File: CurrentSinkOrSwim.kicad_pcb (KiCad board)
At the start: 2 copper layers, 41.7 x 48.5 mm, 26 parts, among them P1 HEATSINK, P101 CONN_01X02, P102 CONN_01X03, P103 CONN_01X02, Q401 BUK9575, U201 LMV358, U301 LM2931

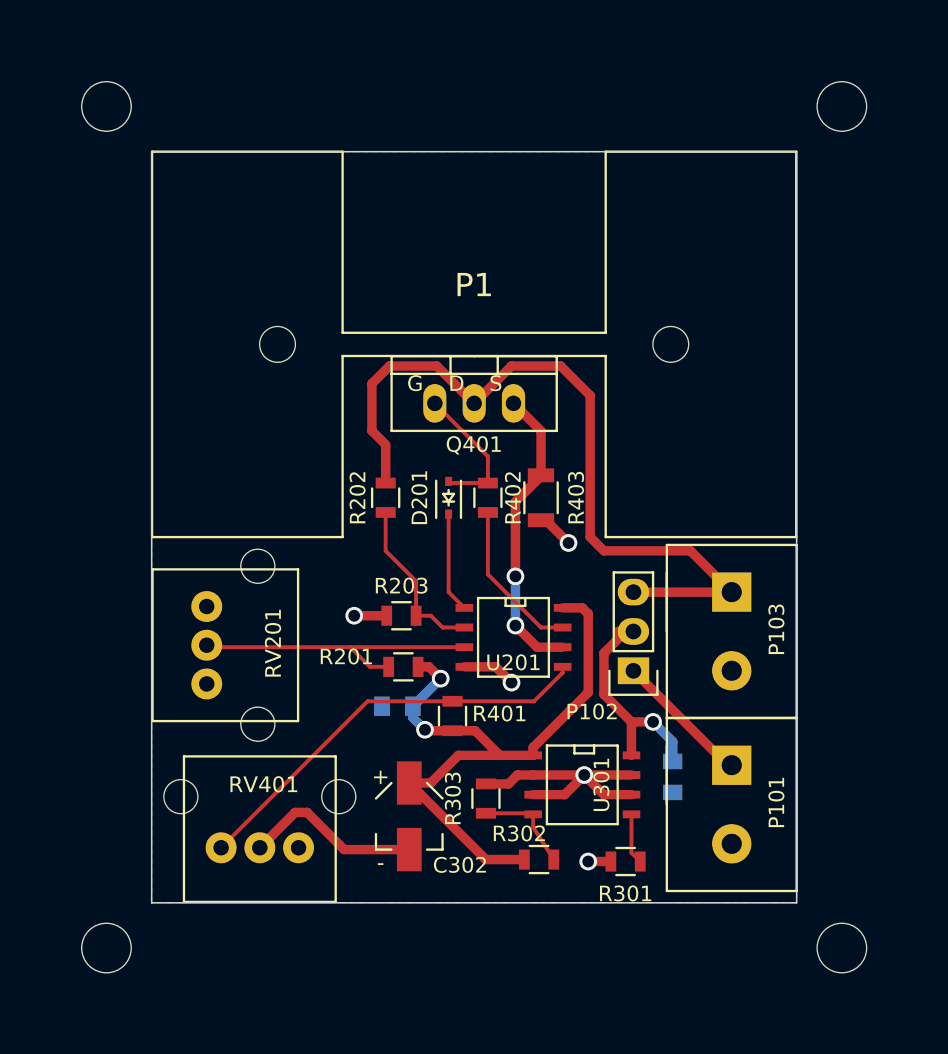
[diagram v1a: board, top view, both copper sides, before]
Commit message: added labels, switched leads on voltage pot so + == clockwise, enlarged ground plane
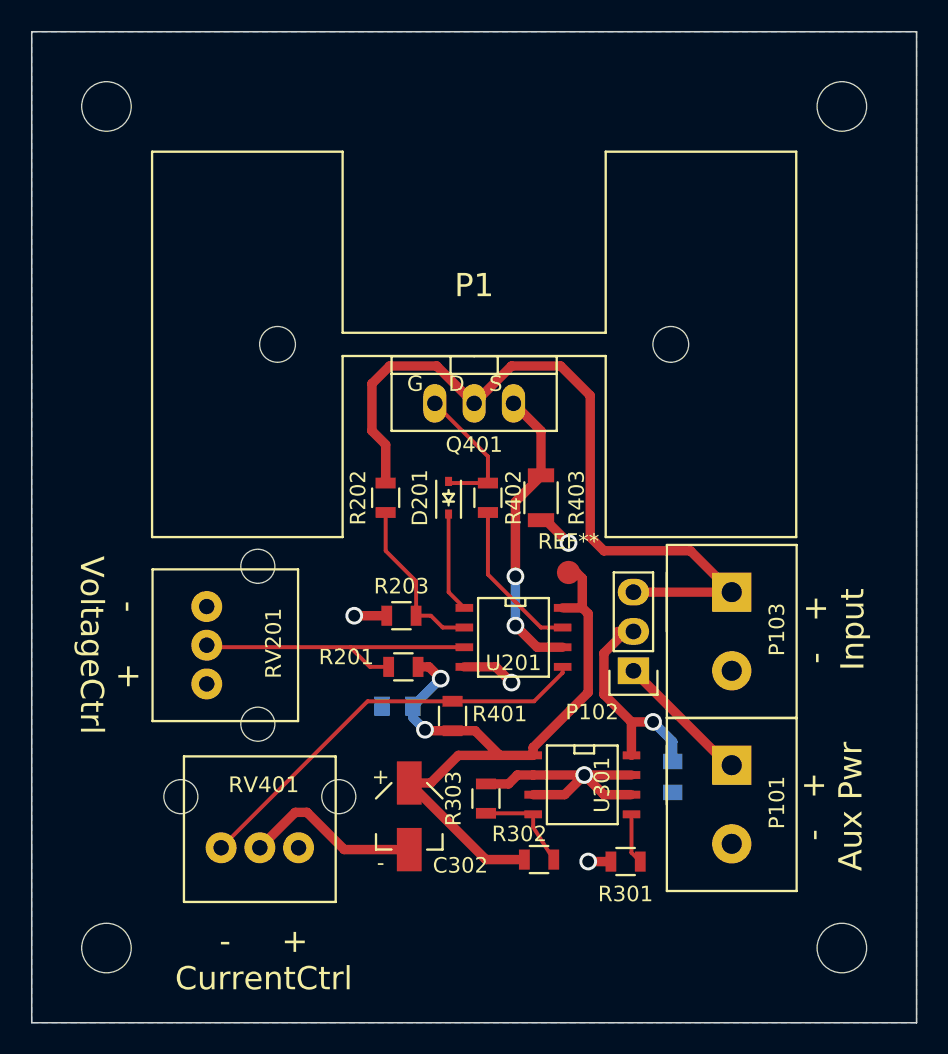
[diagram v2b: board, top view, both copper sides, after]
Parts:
- added REF**: Measurement_Point_Round-SMD-Pad_Small, Measurement_Points:Measurement_Point_Round-SMD-Pad_Small, F.Cu at (133.1, 63.0)
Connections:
- RV201 pad 1: Net-(RV201-Pad1) -> GND
- RV201 pad 3: GND -> Net-(RV201-Pad3)
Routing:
- net 2.7V: track 42.3 -> 45.3 mm
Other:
- board size 41.7 x 48.5 mm -> 57.1 x 64 mm
- board text added: "- + Aux Pwr"
- board text added: "- + CurrentCtrl"
- board text added: "- + Input"
- board text added: "- + VoltageCtrl"
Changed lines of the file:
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@@
 (kicad_pcb (version 4) (host pcbnew 4.0.2-stable)
   (general
-    (links 42)
+    (links 43)
     (no_connects 0)
-    (area 93.260057 27.2092 160.612943 92.5288)
+    (area 93.514057 27.4632 160.485943 92.5288)
     (thickness 1.6)
-    (drawings 4)
-    (tracks 119)
+    (drawings 8)
+    (tracks 123)
     (zones 0)
-    (modules 26)
+    (modules 27)
     (nets 17)
   )
@@
   (layers
     (0 F.Cu signal)
-    (31 B.Cu signal hide)
+    (31 B.Cu signal)
     (32 B.Adhes user)
     (33 F.Adhes user)
@@
     (44 Edge.Cuts user)
     (45 Margin user)
-    (46 B.CrtYd user hide)
+    (46 B.CrtYd user)
     (47 F.CrtYd user)
-    (48 B.Fab user hide)
+    (48 B.Fab user)
     (49 F.Fab user)
   )
@@
     (mod_text_width 0.15)
     (pad_size 1.5 1.5)
-    (pad_drill 0.6)
+    (pad_drill 0)
     (pad_to_mask_clearance 0)
     (aux_axis_origin 0 0)
@@
   (net 13 "Net-(R401-Pad2)")
   (net 14 "Net-(R402-Pad2)")
-  (net 15 "Net-(RV201-Pad1)")
-  (net 16 "Net-(RV401-Pad3)")
+  (net 15 "Net-(RV401-Pad3)")
+  (net 16 "Net-(RV201-Pad3)")
   (net_class Default "This is the default net class."
     (clearance 0.254)
@@
     (add_net "Net-(R401-Pad2)")
     (add_net "Net-(R402-Pad2)")
-    (add_net "Net-(RV201-Pad1)")
+    (add_net "Net-(RV201-Pad3)")
     (add_net "Net-(RV401-Pad3)")
   )
@@
     (add_net "Net-(P101-Pad1)")
     (add_net "Net-(Q401-PadS)")
+  )
+  (module Current:FA-T220-38E (layer F.Cu)
+    (at 127 48.26)
+    (fp_text reference P1 (at 0 -3.81) (layer F.SilkS)
+      (effects (font (size 1.5 1.5) (thickness 0.15)))
+    )
+    (fp_text value HEATSINK (at 0 -6.35) (layer F.Fab)
+      (effects (font (size 1.5 1.5) (thickness 0.15)))
+    )
+    (fp_line (start -8.4963 12.446) (end -20.8026 12.446) (layer F.SilkS) (width 0.15))
+    (fp_line (start 20.8026 12.446) (end 8.4963 12.446) (layer F.SilkS) (width 0.15))
+    (fp_line (start 8.4963 -12.446) (end 20.8026 -12.446) (layer F.SilkS) (width 0.15))
+    (fp_line (start -20.8026 -12.446) (end -8.4963 -12.446) (layer F.SilkS) (width 0.15))
+    (fp_line (start 8.4963 0.7493) (end 8.4963 12.446) (layer F.SilkS) (width 0.15))
+    (fp_line (start -8.4963 0.7493) (end -8.4963 12.446) (layer F.SilkS) (width 0.15))
+    (fp_line (start -8.4963 -0.7493) (end -8.4963 -12.446) (layer F.SilkS) (width 0.15))
+    (fp_line (start 8.4963 -0.7493) (end 8.4963 -12.446) (layer F.SilkS) (width 0.15))
+    (fp_line (start -8.4963 0.7493) (end 8.4963 0.7493) (layer F.SilkS) (width 0.15))
+    (fp_line (start -8.4963 -0.7493) (end 8.4963 -0.7493) (layer F.SilkS) (width 0.15))
+    (fp_line (start 20.8026 -12.446) (end 20.8026 12.446) (layer F.SilkS) (width 0.15))
+    (fp_line (start -20.8026 12.446) (end -20.8026 -12.446) (layer F.SilkS) (width 0.15))
+    (pad "" np_thru_hole circle (at -12.7 0) (size 2.3114 2.3114) (drill 2.3114) (layers *.Cu *.Mask F.SilkS))
+    (pad "" np_thru_hole circle (at 12.7 0) (size 2.3114 2.3114) (drill 2.3114) (layers *.Cu *.Mask F.SilkS))
   )
   (module Current:Terminal_Block_200_mil (layer F.Cu)
@@
       (rotate (xyz 0 0 180))
     )
-  )
-  (module Current:FA-T220-38E (layer F.Cu)
-    (at 127 48.26)
-    (fp_text reference P1 (at 0 -3.81) (layer F.SilkS)
-      (effects (font (size 1.5 1.5) (thickness 0.15)))
-    )
-    (fp_text value HEATSINK (at 0 -6.35) (layer F.Fab)
-      (effects (font (size 1.5 1.5) (thickness 0.15)))
-    )
-    (fp_line (start -8.4963 12.446) (end -20.8026 12.446) (layer F.SilkS) (width 0.15))
-    (fp_line (start 20.8026 12.446) (end 8.4963 12.446) (layer F.SilkS) (width 0.15))
-    (fp_line (start 8.4963 -12.446) (end 20.8026 -12.446) (layer F.SilkS) (width 0.15))
-    (fp_line (start -20.8026 -12.446) (end -8.4963 -12.446) (layer F.SilkS) (width 0.15))
-    (fp_line (start 8.4963 0.7493) (end 8.4963 12.446) (layer F.SilkS) (width 0.15))
-    (fp_line (start -8.4963 0.7493) (end -8.4963 12.446) (layer F.SilkS) (width 0.15))
-    (fp_line (start -8.4963 -0.7493) (end -8.4963 -12.446) (layer F.SilkS) (width 0.15))
-    (fp_line (start 8.4963 -0.7493) (end 8.4963 -12.446) (layer F.SilkS) (width 0.15))
-    (fp_line (start -8.4963 0.7493) (end 8.4963 0.7493) (layer F.SilkS) (width 0.15))
-    (fp_line (start -8.4963 -0.7493) (end 8.4963 -0.7493) (layer F.SilkS) (width 0.15))
-    (fp_line (start 20.8026 -12.446) (end 20.8026 12.446) (layer F.SilkS) (width 0.15))
-    (fp_line (start -20.8026 12.446) (end -20.8026 -12.446) (layer F.SilkS) (width 0.15))
-    (pad "" np_thru_hole circle (at -12.7 0) (size 2.3114 2.3114) (drill 2.3114) (layers *.Cu *.Mask F.SilkS))
-    (pad "" np_thru_hole circle (at 12.7 0) (size 2.3114 2.3114) (drill 2.3114) (layers *.Cu *.Mask F.SilkS))
   )
   (module Current:Terminal_Block_200_mil (layer F.Cu)
@@
     (fp_line (start -4.9 -5.9) (end -4.9 3.5) (layer F.SilkS) (width 0.15))
     (pad 3 thru_hole circle (at 2.5 0 270) (size 2 2) (drill 1) (layers *.Cu *.Mask F.SilkS)
-      (net 2 GND))
+      (net 16 "Net-(RV201-Pad3)"))
     (pad 2 thru_hole circle (at 0 0 270) (size 2 2) (drill 1) (layers *.Cu *.Mask F.SilkS)
       (net 9 "Net-(R201-Pad2)"))
     (pad 1 thru_hole circle (at -2.5 0 270) (size 2 2) (drill 1) (layers *.Cu *.Mask F.SilkS)
-      (net 15 "Net-(RV201-Pad1)"))
+      (net 2 GND))
     (pad "" np_thru_hole circle (at 5.1 -3.3 270) (size 2.2 2.2) (drill 2.2) (layers *.Cu *.Mask F.SilkS))
     (pad "" np_thru_hole circle (at -5.1 -3.3 270) (size 2.2 2.2) (drill 2.2) (layers *.Cu *.Mask F.SilkS))
@@
     (fp_line (start -4.9 -5.9) (end -4.9 3.5) (layer F.SilkS) (width 0.15))
     (pad 3 thru_hole circle (at 2.5 0) (size 2 2) (drill 1) (layers *.Cu *.Mask F.SilkS)
-      (net 16 "Net-(RV401-Pad3)"))
+      (net 15 "Net-(RV401-Pad3)"))
     (pad 2 thru_hole circle (at 0 0) (size 2 2) (drill 1) (layers *.Cu *.Mask F.SilkS)
       (net 2 GND))
@@
     (pad 1 np_thru_hole circle (at 0 0) (size 3.2 3.2) (drill 3.2) (layers *.Cu *.Mask F.SilkS))
   )
-  (gr_line (start 147.828 35.814) (end 106.172 35.814) (angle 90) (layer Edge.Cuts) (width 0.1))
-  (gr_line (start 147.828 84.328) (end 147.828 35.814) (angle 90) (layer Edge.Cuts) (width 0.1))
-  (gr_line (start 106.172 84.328) (end 147.828 84.328) (angle 90) (layer Edge.Cuts) (width 0.1))
-  (gr_line (start 106.172 35.814) (end 106.172 84.328) (angle 90) (layer Edge.Cuts) (width 0.1))
+  (module Measurement_Points:Measurement_Point_Round-SMD-Pad_Small (layer F.Cu)
+    (at 133.096 62.992)
+    (descr "Mesurement Point, Round, SMD Pad, DM 1.5mm,")
+    (tags "Mesurement Point Round SMD Pad 1.5mm")
+    (attr virtual)
+    (fp_text reference REF** (at 0 -2) (layer F.SilkS)
+      (effects (font (size 1 1) (thickness 0.15)))
+    )
+    (fp_text value Measurement_Point_Round-SMD-Pad_Small (at 0 2) (layer F.Fab)
+      (effects (font (size 1 1) (thickness 0.15)))
+    )
+    (fp_circle (center 0 0) (end 1 0) (layer F.CrtYd) (width 0.05))
+    (pad 1 smd circle (at 0 0) (size 1.5 1.5) (layers F.Cu F.Mask)
+      (net 1 2.7V))
+  )
+  (gr_text "-     +\nVoltageCtrl" (at 103.505 67.691 270) (layer F.SilkS)
+    (effects (font (size 1.5 1.5) (thickness 0.3)))
+  )
+  (gr_text "-     +\nCurrentCtrl" (at 113.411 88.011) (layer F.SilkS)
+    (effects (font (size 1.5 1.5) (thickness 0.3)))
+  )
+  (gr_text "-   +\nInput" (at 150.241 66.675 90) (layer F.SilkS)
+    (effects (font (size 1.5 1.5) (thickness 0.3)))
+  )
+  (gr_text "-   +\nAux Pwr" (at 150.114 78.105 90) (layer F.SilkS)
+    (effects (font (size 1.5 1.5) (thickness 0.3)))
+  )
+  (gr_line (start 155.575 28.067) (end 155.575 92.075) (angle 90) (layer Edge.Cuts) (width 0.1))
+  (gr_line (start 98.425 92.075) (end 98.425 28.067) (angle 90) (layer Edge.Cuts) (width 0.1))
+  (gr_line (start 155.575 92.075) (end 98.425 92.075) (angle 90) (layer Edge.Cuts) (width 0.1))
+  (gr_line (start 98.425 28.067) (end 155.575 28.067) (angle 90) (layer Edge.Cuts) (width 0.1))
+  (segment (start 133.096 62.992) (end 133.604 62.992) (width 0.6096) (layer F.Cu) (net 1))
+  (segment (start 133.604 62.992) (end 133.985 63.373) (width 0.6096) (layer F.Cu) (net 1))
+  (segment (start 133.985 63.373) (end 133.985 65.278) (width 0.6096) (layer F.Cu) (net 1))
   (segment (start 123.047 71.628) (end 123.063 71.628) (width 0.6096) (layer B.Cu) (net 1))
   (segment (start 123.063 71.628) (end 124.841 69.85) (width 0.6096) (layer B.Cu) (net 1))
@@
   (segment (start 129.54 52.07) (end 131.318 53.848) (width 0.6096) (layer F.Cu) (net 8))
   (segment (start 131.318 53.848) (end 131.318 56.716) (width 0.6096) (layer F.Cu) (net 8))
+  (segment (start 118.999 67.818) (end 109.855 67.818) (width 0.254) (layer F.Cu) (net 9))
+  (segment (start 109.855 67.818) (end 109.728 67.691) (width 0.254) (layer F.Cu) (net 9))
   (segment (start 121.478 69.088) (end 120.269 69.088) (width 0.254) (layer F.Cu) (net 9))
   (segment (start 120.269 69.088) (end 118.999 67.818) (width 0.254) (layer F.Cu) (net 9))
   (segment (start 126.365 67.818) (end 118.999 67.818) (width 0.254) (layer F.Cu) (net 9))
-  (segment (start 118.999 67.818) (end 109.855 67.818) (width 0.254) (layer F.Cu) (net 9))
   (segment (start 109.855 67.818) (end 109.728 67.691) (width 0.254) (layer F.Cu) (net 9))
   (segment (start 121.285 59.116) (end 121.285 61.595) (width 0.254) (layer F.Cu) (net 10))
@@
     (polygon
       (pts
-        (xy 147.828 84.328) (xy 106.172 84.328) (xy 106.172 35.814) (xy 147.828 35.814) (xy 147.828 84.328)
+        (xy 147.828 92.075) (xy 98.425 92.075) (xy 98.425 28.067) (xy 155.575 28.067) (xy 155.575 84.328)
+        (xy 155.575 92.075)
       )
     )

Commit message: added test points to  schematic and pcb
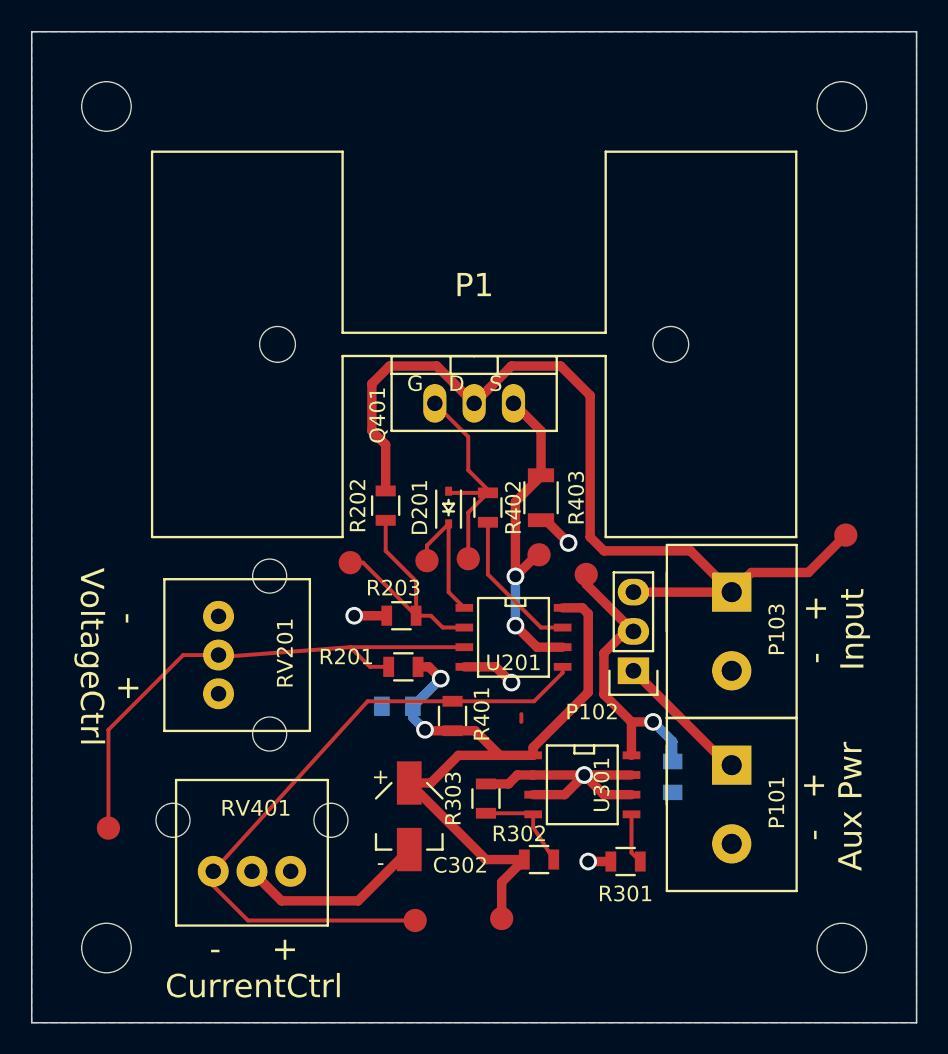
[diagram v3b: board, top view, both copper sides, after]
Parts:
- removed the REF** at (133.1, 63.0)
- added W101: TEST_1P, Measurement_Points:Measurement_Point_Round-SMD-Pad_Small, F.Cu at (151.0, 60.6)
- added W201: TEST_1P, Measurement_Points:Measurement_Point_Round-SMD-Pad_Small, F.Cu at (103.4, 79.5)
- added W202: TEST_1P, Measurement_Points:Measurement_Point_Round-SMD-Pad_Small, F.Cu at (124.0, 62.2)
- added W203: TEST_1P, Measurement_Points:Measurement_Point_Round-SMD-Pad_Small, F.Cu at (119.0, 62.4)
- added W301: TEST_1P, Measurement_Points:Measurement_Point_Round-SMD-Pad_Small, F.Cu at (134.2, 63.1)
- added W302: TEST_1P, Measurement_Points:Measurement_Point_Round-SMD-Pad_Small, F.Cu at (128.8, 85.3)
- added W401: TEST_1P, Measurement_Points:Measurement_Point_Round-SMD-Pad_Small, F.Cu at (123.2, 85.5)
- added W402: TEST_1P, Measurement_Points:Measurement_Point_Round-SMD-Pad_Small, F.Cu at (131.2, 61.8)
- added W403: TEST_1P, Measurement_Points:Measurement_Point_Round-SMD-Pad_Small, F.Cu at (126.6, 62.1)
- moved RV401 1.61 mm to (112.6, 82.3)
- moved RV201 0.99 mm to (110.5, 68.3)
- moved D201 0.64 mm to (125.3, 58.8)
- moved R402 0.64 mm to (127.9, 58.8)
- moved R202 0.51 mm to (121.3, 58.7)
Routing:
- net Net-(R401-Pad2): track 27.2 -> 43.6 mm
- net Net-(R201-Pad2): track 19.9 -> 34.6 mm
- net /Current Control/Current_Sink+: track 50.3 -> 59.7 mm
- net /Current Control/FET_Gate: track 9.69 -> 15.1 mm
- net Net-(R202-Pad2): track 10.9 -> 16.1 mm
- net /Power Regulation/Vin: track 15.3 -> 19.2 mm
- net Net-(D201-Pad1): track 6.48 -> 8.80 mm
- net Net-(Q401-PadS): track 19.4 -> 21.5 mm
- net 2.7V: track 45.3 -> 46.7 mm
- net GND: track 38.2 -> 38.9 mm
- net Net-(R402-Pad2): track 10.2 -> 9.61 mm
- net (no net): track 0.00 -> 0.51 mm

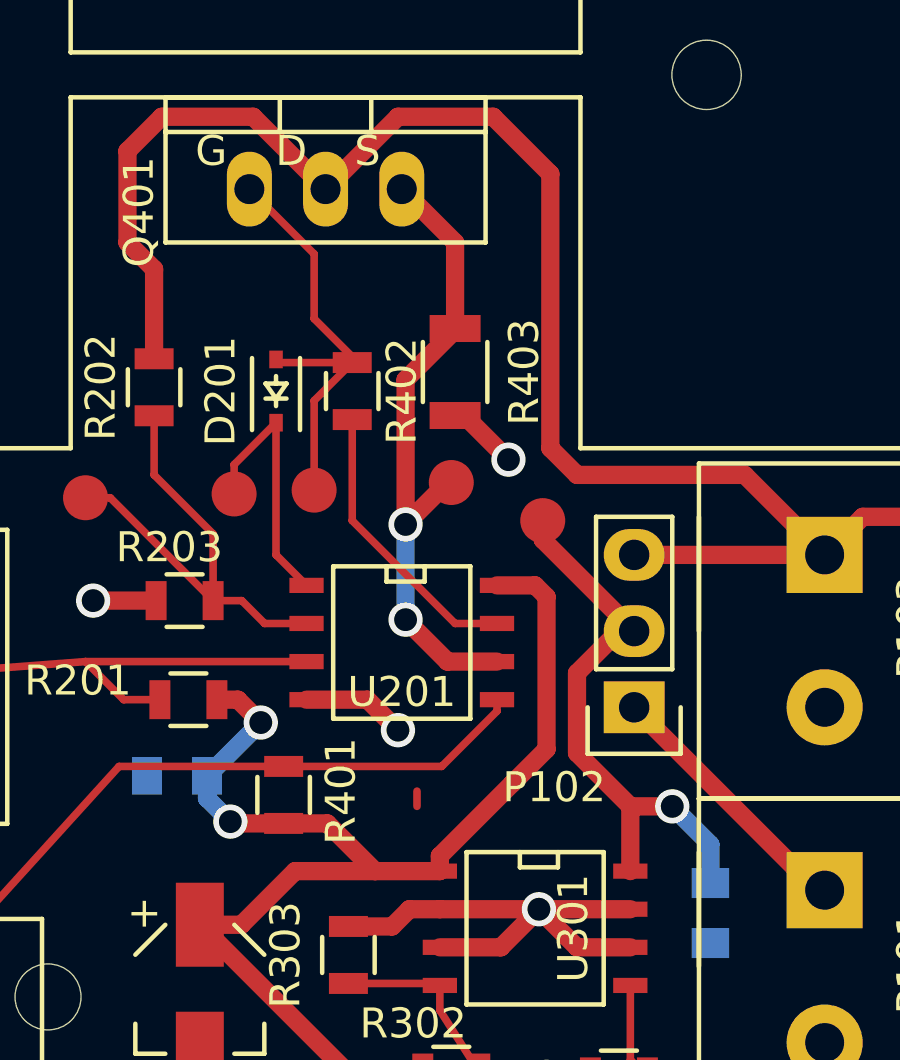
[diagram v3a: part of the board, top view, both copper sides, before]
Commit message: changed sense resistor to 2W, 2512SMD2
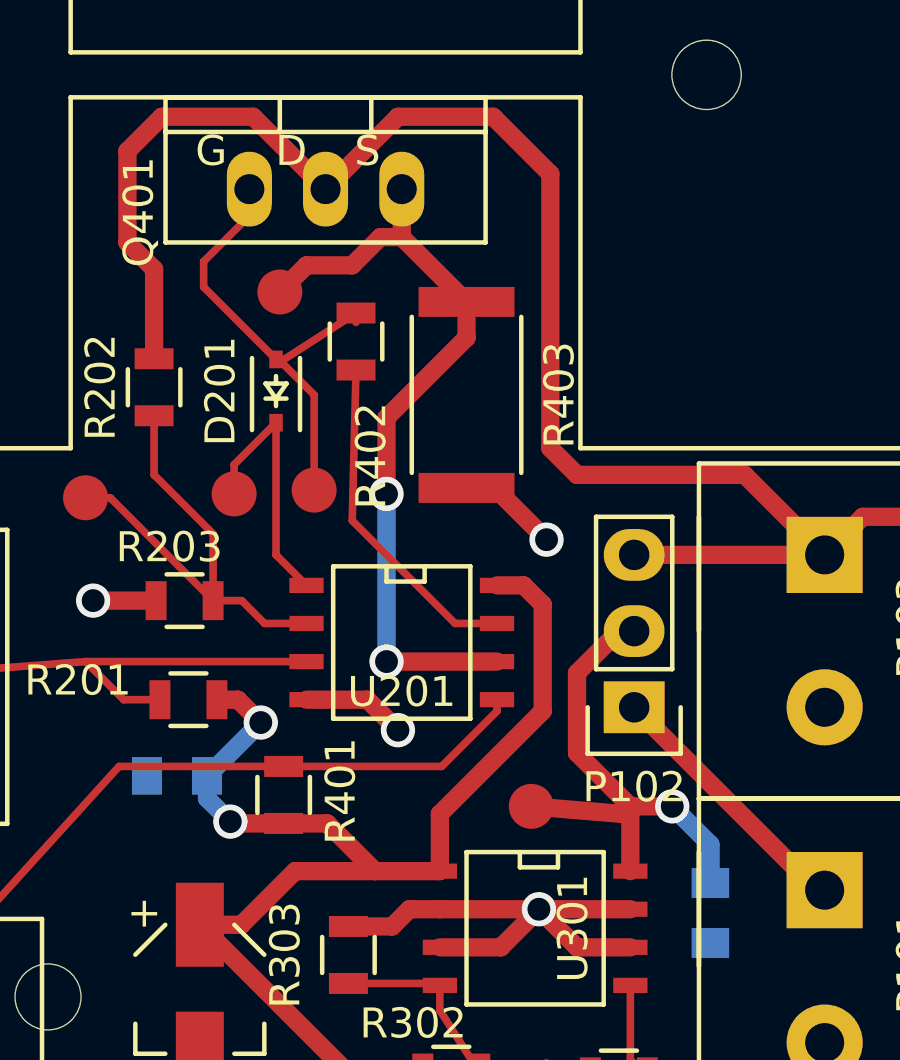
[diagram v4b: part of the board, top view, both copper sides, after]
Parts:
- R403: footprint Resistors_SMD:R_1206 -> Resistors_SMD:R_2512
- moved W301 9.53 mm to (133.9, 72.6)
- moved W402 8.54 mm to (125.5, 55.5)
- moved R402 1.66 mm to (128.0, 57.1)
- moved R403 0.85 mm to (131.7, 58.9)
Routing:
- net Net-(Q401-PadS): track 21.5 -> 26.3 mm
- net GND: track 38.9 -> 41.0 mm
- net Net-(R402-Pad2): track 9.61 -> 11.3 mm
- net /Power Regulation/Vin: track 19.2 -> 17.7 mm
- net /Current Control/FET_Gate: track 15.1 -> 16.5 mm
- net (no net): track 0.51 -> 0.00 mm
